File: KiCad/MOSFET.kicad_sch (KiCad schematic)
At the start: 5 parts, among them J5 Screw_Terminal_01x02, Q1 IRLZ44N

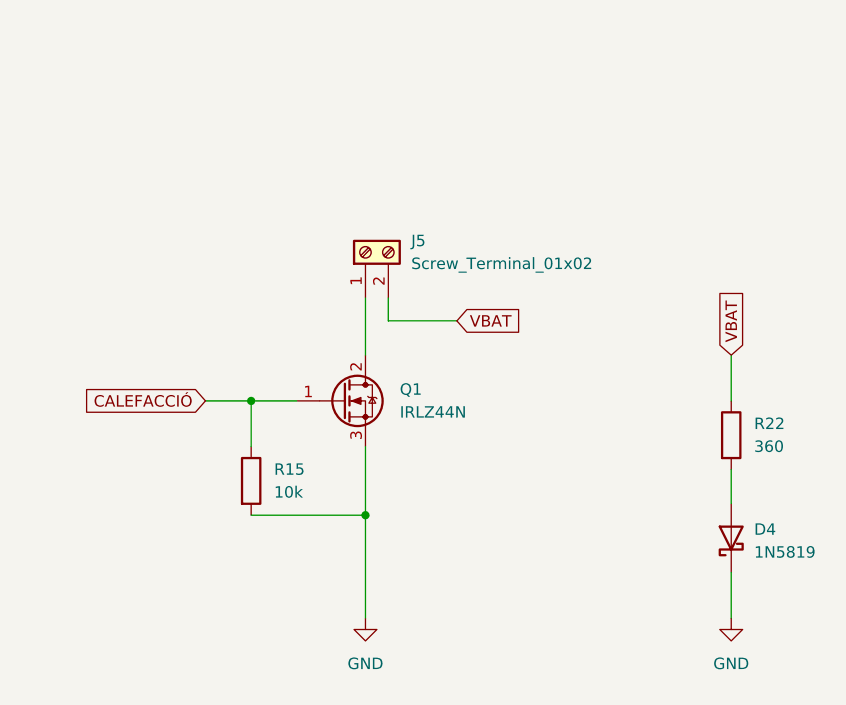
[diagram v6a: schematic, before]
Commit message: Començat el LAYOUT
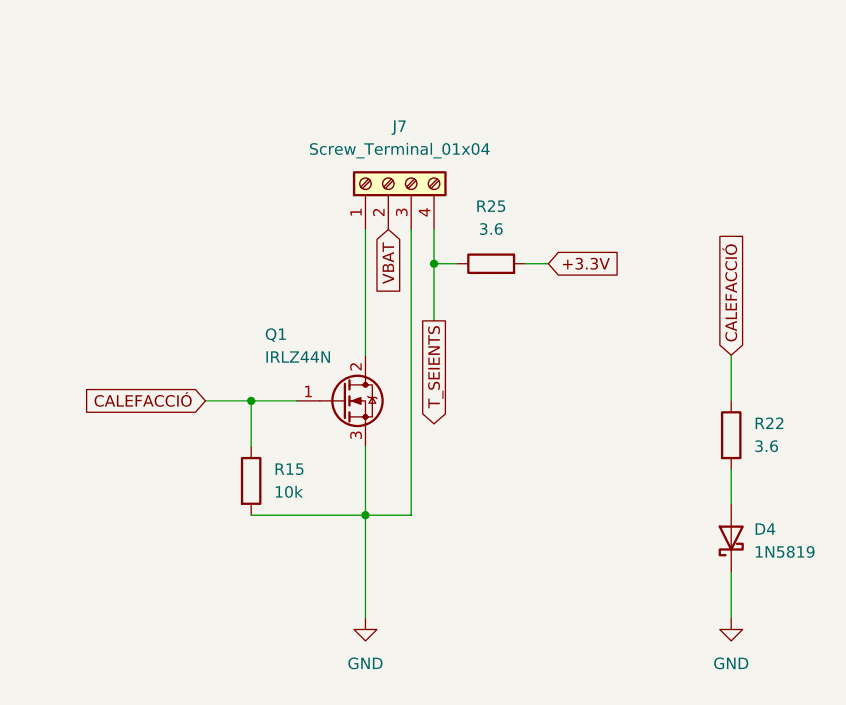
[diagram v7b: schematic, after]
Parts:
- removed J5: Screw_Terminal_01x02, symbol Connector:Screw_Terminal_01x02
- added J7: Screw_Terminal_01x04, symbol Connector:Screw_Terminal_01x04
- added R25: 3.6, Resistor_SMD:R_0805_2012Metric, symbol Device:R
- R15: footprint (none) -> Resistor_SMD:R_0805_2012Metric
- R22: value 360 -> 3.6; footprint (none) -> Resistor_SMD:R_0805_2012Metric
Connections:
- net CALEFACCIÓ: now also R22.1
- net GND: now also J7.3 (Pin_3)
- net VBAT: now also J7.2 (Pin_2); no longer R22.1
- net at Q1.2 (D): now also J7.1 (Pin_1)
- new net +3.3V: R25.2
- new net T_SEIENTS: J7.4 (Pin_4), R25.1
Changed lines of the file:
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@@
 		(color 0 0 0 0)
 	)
-	(wire
-		(pts
-			(xy 148.59 77.47) (xy 148.59 80.01)
+	(junction
+		(at 153.67 73.66)
+		(diameter 0)
+		(color 0 0 0 0)
+	)
+	(wire
+		(pts
+			(xy 151.13 69.85) (xy 151.13 101.6)
+		)
+		(stroke
+			(width 0)
+			(type default)
+		)
+	)
+	(wire
+		(pts
+			(xy 163.83 73.66) (xy 166.37 73.66)
+		)
+		(stroke
+			(width 0)
+			(type default)
+		)
+	)
+	(wire
+		(pts
+			(xy 153.67 73.66) (xy 156.21 73.66)
 		)
 		(stroke
@@
 	(wire
 		(pts
-			(xy 148.59 80.01) (xy 156.21 80.01)
-		)
-		(stroke
-			(width 0)
-			(type default)
-		)
-	)
-	(wire
-		(pts
 			(xy 186.69 83.82) (xy 186.69 88.9)
 		)
@@
 	(wire
 		(pts
-			(xy 146.05 77.47) (xy 146.05 83.82)
+			(xy 146.05 69.85) (xy 146.05 83.82)
 		)
 		(stroke
@@
 	(wire
 		(pts
+			(xy 153.67 69.85) (xy 153.67 73.66)
+		)
+		(stroke
+			(width 0)
+			(type default)
+		)
+	)
+	(wire
+		(pts
 			(xy 133.35 101.6) (xy 146.05 101.6)
 		)
@@
 	(wire
 		(pts
+			(xy 186.69 107.95) (xy 186.69 113.03)
+		)
+		(stroke
+			(width 0)
+			(type default)
+		)
+	)
+	(wire
+		(pts
+			(xy 151.13 101.6) (xy 146.05 101.6)
+		)
+		(stroke
+			(width 0)
+			(type default)
+		)
+	)
+	(wire
+		(pts
 			(xy 146.05 101.6) (xy 146.05 113.03)
 		)
@@
 	(wire
 		(pts
-			(xy 186.69 107.95) (xy 186.69 113.03)
+			(xy 153.67 73.66) (xy 153.67 80.01)
 		)
 		(stroke
@@
 	(global_label "VBAT"
 		(shape input)
-		(at 156.21 80.01 0)
+		(at 148.59 69.85 270)
 		(fields_autoplaced yes)
 		(effects
@@
 				(size 1.27 1.27)
 			)
-			(justify left)
+			(justify right)
 		)
 		(property "Intersheetrefs" "${INTERSHEET_REFS}"
-			(at 163.61 80.01 0)
-			(effects
-				(font
-					(size 1.27 1.27)
-				)
-				(justify left)
+			(at 148.59 76.5958 90)
+			(effects
+				(font
+					(size 1.27 1.27)
+				)
+				(justify right)
 				(hide yes)
 			)
@@
 		)
 	)
-	(global_label "VBAT"
-		(shape input)
-		(at 186.69 83.82 90)
+	(global_label "T_SEIENTS"
+		(shape output)
+		(at 153.67 80.01 270)
 		(fields_autoplaced yes)
 		(effects
@@
 				(size 1.27 1.27)
 			)
+			(justify right)
+		)
+		(property "Intersheetrefs" "${INTERSHEET_REFS}"
+			(at 153.67 91.8961 90)
+			(effects
+				(font
+					(size 1.27 1.27)
+				)
+				(justify right)
+				(hide yes)
+			)
+		)
+	)
+	(global_label "CALEFACCIÓ"
+		(shape input)
+		(at 186.69 83.82 90)
+		(fields_autoplaced yes)
+		(effects
+			(font
+				(size 1.27 1.27)
+			)
 			(justify left)
 		)
 		(property "Intersheetrefs" "${INTERSHEET_REFS}"
-			(at 186.69 76.42 90)
+			(at 186.69 70.3008 90)
+			(effects
+				(font
+					(size 1.27 1.27)
+				)
+				(justify left)
+				(hide yes)
+			)
+		)
+	)
+	(global_label "+3.3V"
+		(shape input)
+		(at 166.37 73.66 0)
+		(fields_autoplaced yes)
+		(effects
+			(font
+				(size 1.27 1.27)
+			)
+			(justify left)
+		)
+		(property "Intersheetrefs" "${INTERSHEET_REFS}"
+			(at 174.3858 73.66 0)
 			(effects
 				(font
@@
 			)
 		)
-		(property "Footprint" ""
+		(property "Footprint" "Resistor_SMD:R_0805_2012Metric"
 			(at 131.572 97.79 90)
 			(effects
@@
 			)
 		)
-		(property "Value" "360"
+		(property "Value" "3.6"
 			(at 189.23 93.9799 0)
 			(effects
@@
 			)
 		)
-		(property "Footprint" ""
+		(property "Footprint" "Resistor_SMD:R_0805_2012Metric"
 			(at 184.912 92.71 90)
 			(effects
@@
 		(on_board yes)
 		(dnp no)
-		(fields_autoplaced yes)
 		(property "Reference" "Q1"
-			(at 149.86 87.6299 0)
+			(at 134.874 81.534 0)
 			(effects
 				(font
@@
 		)
 		(property "Value" "IRLZ44N"
-			(at 149.86 90.1699 0)
+			(at 134.874 84.074 0)
 			(effects
 				(font
@@
 				(path "/b6401b4f-5426-49b8-bb2e-8ecdb19989ef/df19026d-ff61-4139-84bd-7b499d6482c5"
 					(reference "Q1")
+					(unit 1)
+				)
+			)
+		)
+	)
+	(symbol
+		(lib_id "Device:R")
+		(at 160.02 73.66 90)
+		(unit 1)
+		(exclude_from_sim no)
+		(in_bom yes)
+		(on_board yes)
+		(dnp no)
+		(fields_autoplaced yes)
+		(property "Reference" "R25"
+			(at 160.02 67.31 90)
+			(effects
+				(font
+					(size 1.27 1.27)
+				)
+			)
+		)
+		(property "Value" "3.6"
+			(at 160.02 69.85 90)
+			(effects
+				(font
+					(size 1.27 1.27)
+				)
+			)
+		)
+		(property "Footprint" "Resistor_SMD:R_0805_2012Metric"
+			(at 160.02 75.438 90)
+			(effects
+				(font
+					(size 1.27 1.27)
+				)
+				(hide yes)
+			)
+		)
+		(property "Datasheet" "~"
+			(at 160.02 73.66 0)
+			(effects
+				(font
+					(size 1.27 1.27)
+				)
+				(hide yes)
+			)
+		)
+		(property "Description" "Resistor"
+			(at 160.02 73.66 0)
+			(effects
+				(font
+					(size 1.27 1.27)
+				)
+				(hide yes)
+			)
+		)
+		(pin "1"
+		)
+		(pin "2"
+		)
+		(instances
+			(project "SEIENTS_EDD"
+				(path "/b6401b4f-5426-49b8-bb2e-8ecdb19989ef/df19026d-ff61-4139-84bd-7b499d6482c5"
+					(reference "R25")
 					(unit 1)
 				)
@@
 	)
 	(symbol
-		(lib_id "Connector:Screw_Terminal_01x02")
-		(at 146.05 72.39 90)
+		(lib_id "Connector:Screw_Terminal_01x04")
+		(at 148.59 64.77 90)
 		(unit 1)
 		(exclude_from_sim no)
@@
 		(dnp no)
 		(fields_autoplaced yes)
-		(property "Reference" "J5"
-			(at 151.13 71.1199 90)
-			(effects
-				(font
-					(size 1.27 1.27)
-				)
-				(justify right)
-			)
-		)
-		(property "Value" "Screw_Terminal_01x02"
-			(at 151.13 73.6599 90)
-			(effects
-				(font
-					(size 1.27 1.27)
-				)
-				(justify right)
+		(property "Reference" "J7"
+			(at 149.86 58.42 90)
+			(effects
+				(font
+					(size 1.27 1.27)
+				)
+			)
+		)
+		(property "Value" "Screw_Terminal_01x04"
+			(at 149.86 60.96 90)
+			(effects
+				(font
+					(size 1.27 1.27)
+				)
 			)
 		)
 		(property "Footprint" ""
-			(at 146.05 72.39 0)
+			(at 148.59 64.77 0)
 			(effects
 				(font
@@
 		)
 		(property "Datasheet" "~"
-			(at 146.05 72.39 0)
-			(effects
-				(font
-					(size 1.27 1.27)
-				)
-				(hide yes)
-			)
-		)
-		(property "Description" "Generic screw terminal, single row, 01x02, script generated (kicad-library-utils/schlib/autogen/connector/)"
-			(at 146.05 72.39 0)
-			(effects
-				(font
-					(size 1.27 1.27)
-				)
-				(hide yes)
-			)
+			(at 148.59 64.77 0)
+			(effects
+				(font
+					(size 1.27 1.27)
+				)
+				(hide yes)
+			)
+		)
+		(property "Description" "Generic screw terminal, single row, 01x04, script generated (kicad-library-utils/schlib/autogen/connector/)"
+			(at 148.59 64.77 0)
+			(effects
+				(font
+					(size 1.27 1.27)
+				)
+				(hide yes)
+			)
+		)
+		(pin "3"
+		)
+		(pin "1"
+		)
+		(pin "4"
 		)
 		(pin "2"
-		)
-		(pin "1"
 		)
 		(instances
 			(project ""
-				(path "/6381918b-bb9e-4107-aca1-9c14e5889eac"
-					(reference "J66")
-					(unit 1)
-				)
-			)
-			(project "SEIENTS_EDD"
 				(path "/b6401b4f-5426-49b8-bb2e-8ecdb19989ef/df19026d-ff61-4139-84bd-7b499d6482c5"
-					(reference "J5")
-					(unit 1)
-				)
+					(reference "J7")
+					(unit 1)
+				)

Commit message: footprints asignados
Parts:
- J7: footprint (none) -> TerminalBlock_Phoenix:TerminalBlock_Phoenix_MKDS-1,5-4-5.08_1x04_P5.08mm_Horizontal
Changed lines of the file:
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@@
 			)
 		)
-		(property "Footprint" ""
+		(property "Footprint" "TerminalBlock_Phoenix:TerminalBlock_Phoenix_MKDS-1,5-4-5.08_1x04_P5.08mm_Horizontal"
 			(at 148.59 64.77 0)
 			(effects
